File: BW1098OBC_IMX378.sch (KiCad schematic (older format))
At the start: 29 parts, among them J2 24-5804-030-000-829+

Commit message: Update
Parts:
- renumbered 1V05_IMX378_3 to 1V05_IMX378_?, 1V05_IMX378_2 to 1V05_IMX378_?, 1V05_IMX378 to 1V05_IMX?, 1V8_IMX378_3 to 1V8_IMX378_?, 1V8_IMX378_2 to 1V8_IMX378_?, 1V8_IMX378 to 1V8_IMX?, 1V8 to 1V?, 1V05 to 1V?, 2V8_IMX378_3 to 2V8_IMX378_?, 2V8_IMX378_2 to 2V8_IMX378_?, 2V8_IMX378 to 2V8_IMX?, 2V8 to 2V?, 2v8 to 2v?, C3 to C?, C2 to C?, C4 to C?, C5 to C?, C6 to C?, C1 to C?, FB3 to FB?, FB2 to FB?, FB1 to FB?, GND_25 to GND_?, GND_24 to GND_?, GND_23 to GND_?, GND_22 to GND_?, GND_21 to GND_?, J2 to J?, R1 to R?
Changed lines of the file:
@@
 $Descr B 17000 11000
 encoding utf-8
-Sheet 1 1
+Sheet 5 8
 Title "BW1098OBC_IMX378-SchDoc"
 Date "12 12 2020"
@@
 DPHYv1.2
 $Comp
-L power:GND 1V05
+L power:GND 1V?
 U 1 1 5FD53070
 P 1200 1600
-F 0 "1V05" H 1200 1740 20  0000 C CNN
+F 0 "1V?" H 1200 1740 20  0000 C CNN
 F 1 "1V05" H 1200 1710 30  0000 C CNN
 F 2 "" H 1200 1600 70  0000 C CNN
@@
 $EndComp
 $Comp
-L power:GND 2V8
+L power:GND 2V?
 U 1 1 5FD5306F
 P 1200 1000
-F 0 "2V8" H 1200 1140 20  0000 C CNN
+F 0 "2V?" H 1200 1140 20  0000 C CNN
 F 1 "2V8" H 1200 1110 30  0000 C CNN
 F 2 "" H 1200 1000 70  0000 C CNN
@@
 GND
 $Comp
-L power:GND 2V8_IMX378
+L power:GND 2V8_IMX?
 U 1 1 5FD5306E
 P 10000 6900
-F 0 "2V8_IMX378" H 10000 7040 20  0000 C CNN
+F 0 "2V8_IMX?" H 10000 7040 20  0000 C CNN
 F 1 "2V8_IMX378" H 10000 7010 30  0000 C CNN
 F 2 "" H 10000 6900 70  0000 C CNN
@@
 $EndComp
 $Comp
-L power:GND 1V8_IMX378
+L power:GND 1V8_IMX?
 U 1 1 5FD5306D
 P 8700 6900
-F 0 "1V8_IMX378" H 8700 7040 20  0000 C CNN
+F 0 "1V8_IMX?" H 8700 7040 20  0000 C CNN
 F 1 "1V8_IMX378" H 8700 7010 30  0000 C CNN
 F 2 "" H 8700 6900 70  0000 C CNN
@@
 $EndComp
 $Comp
-L power:GND 1V8_IMX378_2
+L power:GND 1V8_IMX378_?
 U 1 1 5FD5306C
 P 7600 5700
-F 0 "1V8_IMX378_2" H 7600 5840 20  0000 C CNN
+F 0 "1V8_IMX378_?" H 7600 5840 20  0000 C CNN
 F 1 "1V8_IMX378" H 7600 5810 30  0000 C CNN
 F 2 "" H 7600 5700 70  0000 C CNN
@@
 $EndComp
 $Comp
-L power:GND GND_21
+L power:GND GND_?
 U 1 1 5FD5306B
 P 11500 5200
-F 0 "GND_21" H 11500 5340 20  0000 C CNN
+F 0 "GND_?" H 11500 5340 20  0000 C CNN
 F 1 "GND" H 11500 5310 30  0000 C CNN
 F 2 "" H 11500 5200 70  0000 C CNN
@@
 $EndComp
 $Comp
-L power:GND GND_22
+L power:GND GND_?
 U 1 1 5FD5306A
 P 1100 1900
-F 0 "GND_22" H 1100 1900 20  0000 C CNN
+F 0 "GND_?" H 1100 1900 20  0000 C CNN
 F 1 "GND" H 1100 1830 30  0000 C CNN
 F 2 "" H 1100 1900 70  0000 C CNN
@@
 $EndComp
 $Comp
-L power:GND GND_23
+L power:GND GND_?
 U 1 1 5FD53069
 P 9000 7400
-F 0 "GND_23" H 9000 7400 20  0000 C CNN
+F 0 "GND_?" H 9000 7400 20  0000 C CNN
 F 1 "GND" H 9000 7330 30  0000 C CNN
 F 2 "" H 9000 7400 70  0000 C CNN
@@
 $EndComp
 $Comp
-L power:GND GND_24
+L power:GND GND_?
 U 1 1 5FD53068
 P 7900 6100
-F 0 "GND_24" H 7900 6100 20  0000 C CNN
+F 0 "GND_?" H 7900 6100 20  0000 C CNN
 F 1 "GND" H 7900 6030 30  0000 C CNN
 F 2 "" H 7900 6100 70  0000 C CNN
@@
 $EndComp
 $Comp
-L power:GND GND_25
+L power:GND GND_?
 U 1 1 5FD53067
 P 9900 6100
-F 0 "GND_25" H 9900 6100 20  0000 C CNN
+F 0 "GND_?" H 9900 6100 20  0000 C CNN
 F 1 "GND" H 9900 6030 30  0000 C CNN
 F 2 "" H 9900 6100 70  0000 C CNN
@@
 1V8
 $Comp
-L power:GND 1V8
+L power:GND 1V?
 U 1 1 5FD53066
 P 1200 1300
-F 0 "1V8" H 1200 1440 20  0000 C CNN
+F 0 "1V?" H 1200 1440 20  0000 C CNN
 F 1 "1V8" H 1200 1410 30  0000 C CNN
 F 2 "" H 1200 1300 70  0000 C CNN
@@
 $EndComp
 $Comp
-L power:GND 1V8_IMX378_3
+L power:GND 1V8_IMX378_?
 U 1 1 5FD53065
 P 2400 1300
-F 0 "1V8_IMX378_3" H 2400 1440 20  0001 C CNN
+F 0 "1V8_IMX378_?" H 2400 1440 20  0001 C CNN
 F 1 "1V8_IMX378" H 2400 1350 30  0000 C CNN
 F 2 "" H 2400 1300 70  0000 C CNN
@@
 $EndComp
 $Comp
-L power:GND 2V8_IMX378_2
+L power:GND 2V8_IMX378_?
 U 1 1 5FD53064
 P 7600 5500
-F 0 "2V8_IMX378_2" H 7600 5640 20  0000 C CNN
+F 0 "2V8_IMX378_?" H 7600 5640 20  0000 C CNN
 F 1 "2V8_IMX378" H 7600 5610 30  0000 C CNN
 F 2 "" H 7600 5500 70  0000 C CNN
@@
 $EndComp
 $Comp
-L power:GND 2V8_IMX378_3
+L power:GND 2V8_IMX378_?
 U 1 1 5FD53063
 P 10100 5700
-F 0 "2V8_IMX378_3" H 10100 5840 20  0000 C CNN
+F 0 "2V8_IMX378_?" H 10100 5840 20  0000 C CNN
 F 1 "2V8_IMX378" H 10100 5810 30  0000 C CNN
 F 2 "" H 10100 5700 70  0000 C CNN
@@
 $EndComp
 $Comp
-L power:GND 2v8
+L power:GND 2v?
 U 1 1 5FD53062
 P 2400 1000
-F 0 "2v8" H 2400 1140 20  0001 C CNN
+F 0 "2v?" H 2400 1140 20  0001 C CNN
 F 1 "2V8_IMX378" H 2400 1050 30  0000 C CNN
 F 2 "" H 2400 1000 70  0000 C CNN
@@
 $EndComp
 $Comp
-L power:GND 1V05_IMX378
+L power:GND 1V05_IMX?
 U 1 1 5FD53061
 P 2400 1600
-F 0 "1V05_IMX378" H 2400 1740 20  0001 C CNN
+F 0 "1V05_IMX?" H 2400 1740 20  0001 C CNN
 F 1 "1V05_IMX378" H 2400 1650 30  0000 C CNN
 F 2 "" H 2400 1600 70  0000 C CNN
@@
 $EndComp
 $Comp
-L power:GND 1V05_IMX378_2
+L power:GND 1V05_IMX378_?
 U 1 1 5FD53060
 P 7400 6900
-F 0 "1V05_IMX378_2" H 7400 7040 20  0000 C CNN
+F 0 "1V05_IMX378_?" H 7400 7040 20  0000 C CNN
 F 1 "1V05_IMX378" H 7400 7010 30  0000 C CNN
 F 2 "" H 7400 6900 70  0000 C CNN
@@
 $EndComp
 $Comp
-L power:GND 1V05_IMX378_3
+L power:GND 1V05_IMX378_?
 U 1 1 5FD5305F
 P 7600 5900
-F 0 "1V05_IMX378_3" H 7600 6040 20  0000 C CNN
+F 0 "1V05_IMX378_?" H 7600 6040 20  0000 C CNN
 F 1 "1V05_IMX378" H 7600 6010 30  0000 C CNN
 F 2 "" H 7600 5900 70  0000 C CNN
@@
 Connection ~ 10000 6900
 $Comp
-L BW1098OBC_IMX378-rescue:2508056017Y2--BW1098OBC_IMX378-SchDoc-rescue FB1
+L BW1098OBC_IMX378-rescue:2508056017Y2--BW1098OBC_IMX378-SchDoc-rescue FB?
 U 1 1 5FD5305E
 P 1400 1000
-F 0 "FB1" H 1500 1050 60  0000 L BNN
+F 0 "FB?" H 1500 1050 60  0000 L BNN
 F 1 "600R/100MHz" H 1500 870 60  0000 L BNN
 F 2 "" H 1500 870 60  0000 C CNN
@@
 $EndComp
 $Comp
-L BW1098OBC_IMX378-rescue:GRM155R71A104JA01D--BW1098OBC_IMX378-SchDoc-rescue C1
+L BW1098OBC_IMX378-rescue:GRM155R71A104JA01D--BW1098OBC_IMX378-SchDoc-rescue C?
 U 1 1 5FD5305D
 P 7400 7200
-F 0 "C1" V 7510 7110 60  0000 R TNN
+F 0 "C?" V 7510 7110 60  0000 R TNN
 F 1 "0.1uF 0402" V 7410 7110 60  0000 R TNN
 F 2 "" H 7410 7110 60  0000 C CNN
@@
 $EndComp
 $Comp
-L BW1098OBC_IMX378-rescue:A12N02A-201_Connector--BW1098OBC_IMX378-SchDoc-rescue J2
+L BW1098OBC_IMX378-rescue:A12N02A-201_Connector--BW1098OBC_IMX378-SchDoc-rescue J?
 U 1 1 5FD5305C
 P 8000 6000
-F 0 "J2" H 8200 7600 60  0000 L BNN
+F 0 "J?" H 8200 7600 60  0000 L BNN
 F 1 "24-5804-030-000-829+" H 8200 5900 60  0000 L BNN
 F 2 "" H 8200 5900 60  0000 C CNN
@@
 $EndComp
 $Comp
-L BW1098OBC_IMX378-rescue:2508056017Y2--BW1098OBC_IMX378-SchDoc-rescue FB2
+L BW1098OBC_IMX378-rescue:2508056017Y2--BW1098OBC_IMX378-SchDoc-rescue FB?
 U 1 1 5FD5305B
 P 1400 1300
-F 0 "FB2" H 1500 1350 60  0000 L BNN
+F 0 "FB?" H 1500 1350 60  0000 L BNN
 F 1 "600R/100MHz" H 1500 1170 60  0000 L BNN
 F 2 "" H 1500 1170 60  0000 C CNN
@@
 $EndComp
 $Comp
-L BW1098OBC_IMX378-rescue:2508056017Y2--BW1098OBC_IMX378-SchDoc-rescue FB3
+L BW1098OBC_IMX378-rescue:2508056017Y2--BW1098OBC_IMX378-SchDoc-rescue FB?
 U 1 1 5FD5305A
 P 1400 1600
-F 0 "FB3" H 1500 1650 60  0000 L BNN
+F 0 "FB?" H 1500 1650 60  0000 L BNN
 F 1 "600R/100MHz" H 1500 1470 60  0000 L BNN
 F 2 "" H 1500 1470 60  0000 C CNN
@@
 $EndComp
 $Comp
-L BW1098OBC_IMX378-rescue:RC0402FR-1310KL--BW1098OBC_IMX378-SchDoc-rescue R1
+L BW1098OBC_IMX378-rescue:RC0402FR-1310KL--BW1098OBC_IMX378-SchDoc-rescue R?
 U 1 1 5FD53059
 P 11000 5200
-F 0 "R1" H 11090 5230 60  0000 L BNN
+F 0 "R?" H 11090 5230 60  0000 L BNN
 F 1 "10K 0402" H 11090 5070 60  0000 L BNN
 F 2 "" H 11090 5070 60  0000 C CNN
@@
 $EndComp
 $Comp
-L BW1098OBC_IMX378-rescue:GRM188R61A106ME69D--BW1098OBC_IMX378-SchDoc-rescue C6
+L BW1098OBC_IMX378-rescue:GRM188R61A106ME69D--BW1098OBC_IMX378-SchDoc-rescue C?
 U 1 1 5FD53058
 P 10600 7200
-F 0 "C6" V 10710 7110 60  0000 R TNN
+F 0 "C?" V 10710 7110 60  0000 R TNN
 F 1 "10uF 0603" V 10610 7110 60  0000 R TNN
 F 2 "" H 10610 7110 60  0000 C CNN
@@
 $EndComp
 $Comp
-L BW1098OBC_IMX378-rescue:GRM155R71A104JA01D--BW1098OBC_IMX378-SchDoc-rescue C5
+L BW1098OBC_IMX378-rescue:GRM155R71A104JA01D--BW1098OBC_IMX378-SchDoc-rescue C?
 U 1 1 5FD53057
 P 10000 7200
-F 0 "C5" V 10110 7110 60  0000 R TNN
+F 0 "C?" V 10110 7110 60  0000 R TNN
 F 1 "0.1uF 0402" V 10010 7110 60  0000 R TNN
 F 2 "" H 10010 7110 60  0000 C CNN
@@
 $EndComp
 $Comp
-L BW1098OBC_IMX378-rescue:GRM188R61A106ME69D--BW1098OBC_IMX378-SchDoc-rescue C4
+L BW1098OBC_IMX378-rescue:GRM188R61A106ME69D--BW1098OBC_IMX378-SchDoc-rescue C?
 U 1 1 5FD53056
 P 9300 7200
-F 0 "C4" V 9410 7110 60  0000 R TNN
+F 0 "C?" V 9410 7110 60  0000 R TNN
 F 1 "10uF 0603" V 9310 7110 60  0000 R TNN
 F 2 "" H 9310 7110 60  0000 C CNN
@@
 $EndComp
 $Comp
-L BW1098OBC_IMX378-rescue:GRM188R61A106ME69D--BW1098OBC_IMX378-SchDoc-rescue C2
+L BW1098OBC_IMX378-rescue:GRM188R61A106ME69D--BW1098OBC_IMX378-SchDoc-rescue C?
 U 1 1 5FD53055
 P 8000 7200
-F 0 "C2" V 8110 7110 60  0000 R TNN
+F 0 "C?" V 8110 7110 60  0000 R TNN
 F 1 "10uF 0603" V 8010 7110 60  0000 R TNN
 F 2 "" H 8010 7110 60  0000 C CNN
@@
 $EndComp
 $Comp
-L BW1098OBC_IMX378-rescue:GRM155R71A104JA01D--BW1098OBC_IMX378-SchDoc-rescue C3
+L BW1098OBC_IMX378-rescue:GRM155R71A104JA01D--BW1098OBC_IMX378-SchDoc-rescue C?
 U 1 1 5FD53054
 P 8700 7200
-F 0 "C3" V 8810 7110 60  0000 R TNN
+F 0 "C?" V 8810 7110 60  0000 R TNN
 F 1 "0.1uF 0402" V 8710 7110 60  0000 R TNN
 F 2 "" H 8710 7110 60  0000 C CNN

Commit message: Cleaned up some duplicates, started reorganizing and putting symbols into one luxonis library so the others can be deleted, added SOM Connector footprint
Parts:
- C? (x3): symbol BW1098OBC_IMX378-rescue:GRM155R71A104JA01D--BW1098OBC_IMX378-SchDoc-rescue -> BW1098OBC_TopLevel-rescue:GRM155R71A104JA01D--BW1098OBC_IMX378-SchDoc-rescue-BW1098OBC_IMX378-rescue
- C? (x3): symbol BW1098OBC_IMX378-rescue:GRM188R61A106ME69D--BW1098OBC_IMX378-SchDoc-rescue -> BW1098OBC_TopLevel-rescue:GRM188R61A106ME69D--BW1098OBC_IMX378-SchDoc-rescue-BW1098OBC_IMX378-rescue
- FB? (x3): symbol BW1098OBC_IMX378-rescue:2508056017Y2--BW1098OBC_IMX378-SchDoc-rescue -> BW1098OBC_TopLevel-rescue:2508056017Y2--BW1098OBC_IMX378-SchDoc-rescue-BW1098OBC_IMX378-rescue
- J?: symbol BW1098OBC_IMX378-rescue:A12N02A-201_Connector--BW1098OBC_IMX378-SchDoc-rescue -> BW1098OBC_TopLevel-rescue:A12N02A-201_Connector--BW1098OBC_IMX378-SchDoc-rescue-BW1098OBC_IMX378-rescue
- R?: symbol BW1098OBC_IMX378-rescue:RC0402FR-1310KL--BW1098OBC_IMX378-SchDoc-rescue -> BW1098OBC_TopLevel-rescue:RC0402FR-1310KL--BW1098OBC_IMX378-SchDoc-rescue-BW1098OBC_IMX378-rescue
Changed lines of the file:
@@
 Connection ~ 10000 6900
 $Comp
-L BW1098OBC_IMX378-rescue:2508056017Y2--BW1098OBC_IMX378-SchDoc-rescue FB?
+L BW1098OBC_TopLevel-rescue:2508056017Y2--BW1098OBC_IMX378-SchDoc-rescue-BW1098OBC_IMX378-rescue FB?
 U 1 1 5FD5305E
 P 1400 1000
@@
 $EndComp
 $Comp
-L BW1098OBC_IMX378-rescue:GRM155R71A104JA01D--BW1098OBC_IMX378-SchDoc-rescue C?
+L BW1098OBC_TopLevel-rescue:GRM155R71A104JA01D--BW1098OBC_IMX378-SchDoc-rescue-BW1098OBC_IMX378-rescue C?
 U 1 1 5FD5305D
 P 7400 7200
@@
 $EndComp
 $Comp
-L BW1098OBC_IMX378-rescue:A12N02A-201_Connector--BW1098OBC_IMX378-SchDoc-rescue J?
+L BW1098OBC_TopLevel-rescue:A12N02A-201_Connector--BW1098OBC_IMX378-SchDoc-rescue-BW1098OBC_IMX378-rescue J?
 U 1 1 5FD5305C
 P 8000 6000
@@
 $EndComp
 $Comp
-L BW1098OBC_IMX378-rescue:2508056017Y2--BW1098OBC_IMX378-SchDoc-rescue FB?
+L BW1098OBC_TopLevel-rescue:2508056017Y2--BW1098OBC_IMX378-SchDoc-rescue-BW1098OBC_IMX378-rescue FB?
 U 1 1 5FD5305B
 P 1400 1300
@@
 $EndComp
 $Comp
-L BW1098OBC_IMX378-rescue:2508056017Y2--BW1098OBC_IMX378-SchDoc-rescue FB?
+L BW1098OBC_TopLevel-rescue:2508056017Y2--BW1098OBC_IMX378-SchDoc-rescue-BW1098OBC_IMX378-rescue FB?
 U 1 1 5FD5305A
 P 1400 1600
@@
 $EndComp
 $Comp
-L BW1098OBC_IMX378-rescue:RC0402FR-1310KL--BW1098OBC_IMX378-SchDoc-rescue R?
+L BW1098OBC_TopLevel-rescue:RC0402FR-1310KL--BW1098OBC_IMX378-SchDoc-rescue-BW1098OBC_IMX378-rescue R?
 U 1 1 5FD53059
 P 11000 5200
@@
 $EndComp
 $Comp
-L BW1098OBC_IMX378-rescue:GRM188R61A106ME69D--BW1098OBC_IMX378-SchDoc-rescue C?
+L BW1098OBC_TopLevel-rescue:GRM188R61A106ME69D--BW1098OBC_IMX378-SchDoc-rescue-BW1098OBC_IMX378-rescue C?
 U 1 1 5FD53058
 P 10600 7200
@@
 $EndComp
 $Comp
-L BW1098OBC_IMX378-rescue:GRM155R71A104JA01D--BW1098OBC_IMX378-SchDoc-rescue C?
+L BW1098OBC_TopLevel-rescue:GRM155R71A104JA01D--BW1098OBC_IMX378-SchDoc-rescue-BW1098OBC_IMX378-rescue C?
 U 1 1 5FD53057
 P 10000 7200
@@
 $EndComp
 $Comp
-L BW1098OBC_IMX378-rescue:GRM188R61A106ME69D--BW1098OBC_IMX378-SchDoc-rescue C?
+L BW1098OBC_TopLevel-rescue:GRM188R61A106ME69D--BW1098OBC_IMX378-SchDoc-rescue-BW1098OBC_IMX378-rescue C?
 U 1 1 5FD53056
 P 9300 7200
@@
 $EndComp
 $Comp
-L BW1098OBC_IMX378-rescue:GRM188R61A106ME69D--BW1098OBC_IMX378-SchDoc-rescue C?
+L BW1098OBC_TopLevel-rescue:GRM188R61A106ME69D--BW1098OBC_IMX378-SchDoc-rescue-BW1098OBC_IMX378-rescue C?
 U 1 1 5FD53055
 P 8000 7200
@@
 $EndComp
 $Comp
-L BW1098OBC_IMX378-rescue:GRM155R71A104JA01D--BW1098OBC_IMX378-SchDoc-rescue C?
+L BW1098OBC_TopLevel-rescue:GRM155R71A104JA01D--BW1098OBC_IMX378-SchDoc-rescue-BW1098OBC_IMX378-rescue C?
 U 1 1 5FD53054
 P 8700 7200

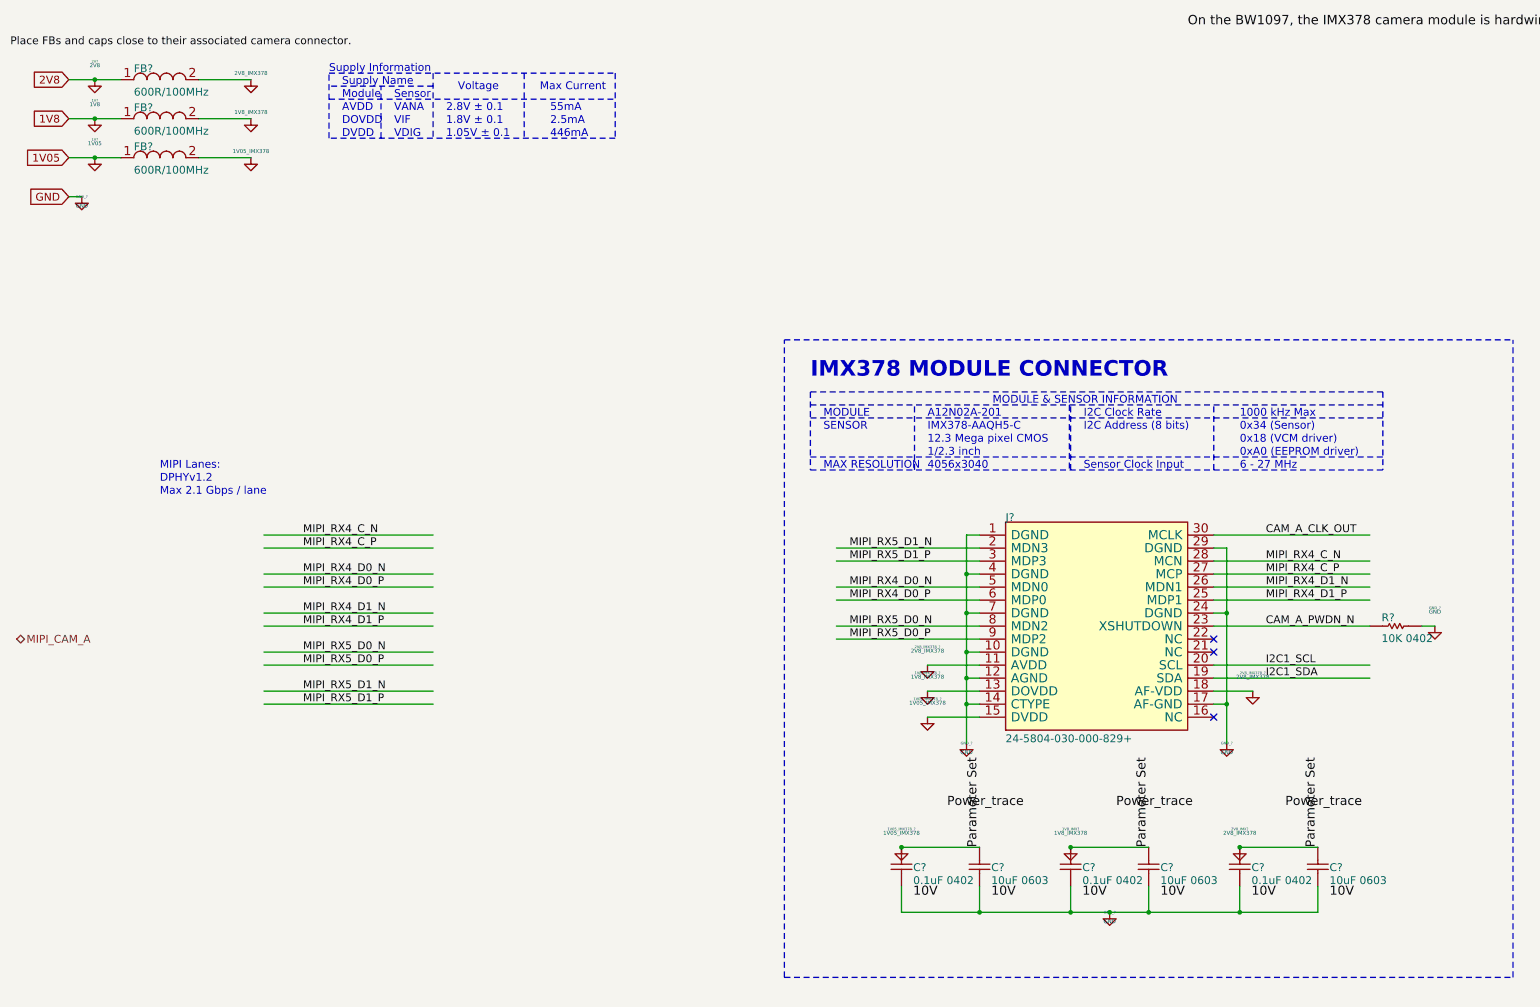
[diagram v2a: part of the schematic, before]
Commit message: More deletion of corrupted or duplicate files, added footprints and associations for mounting holes and 30 pin connector
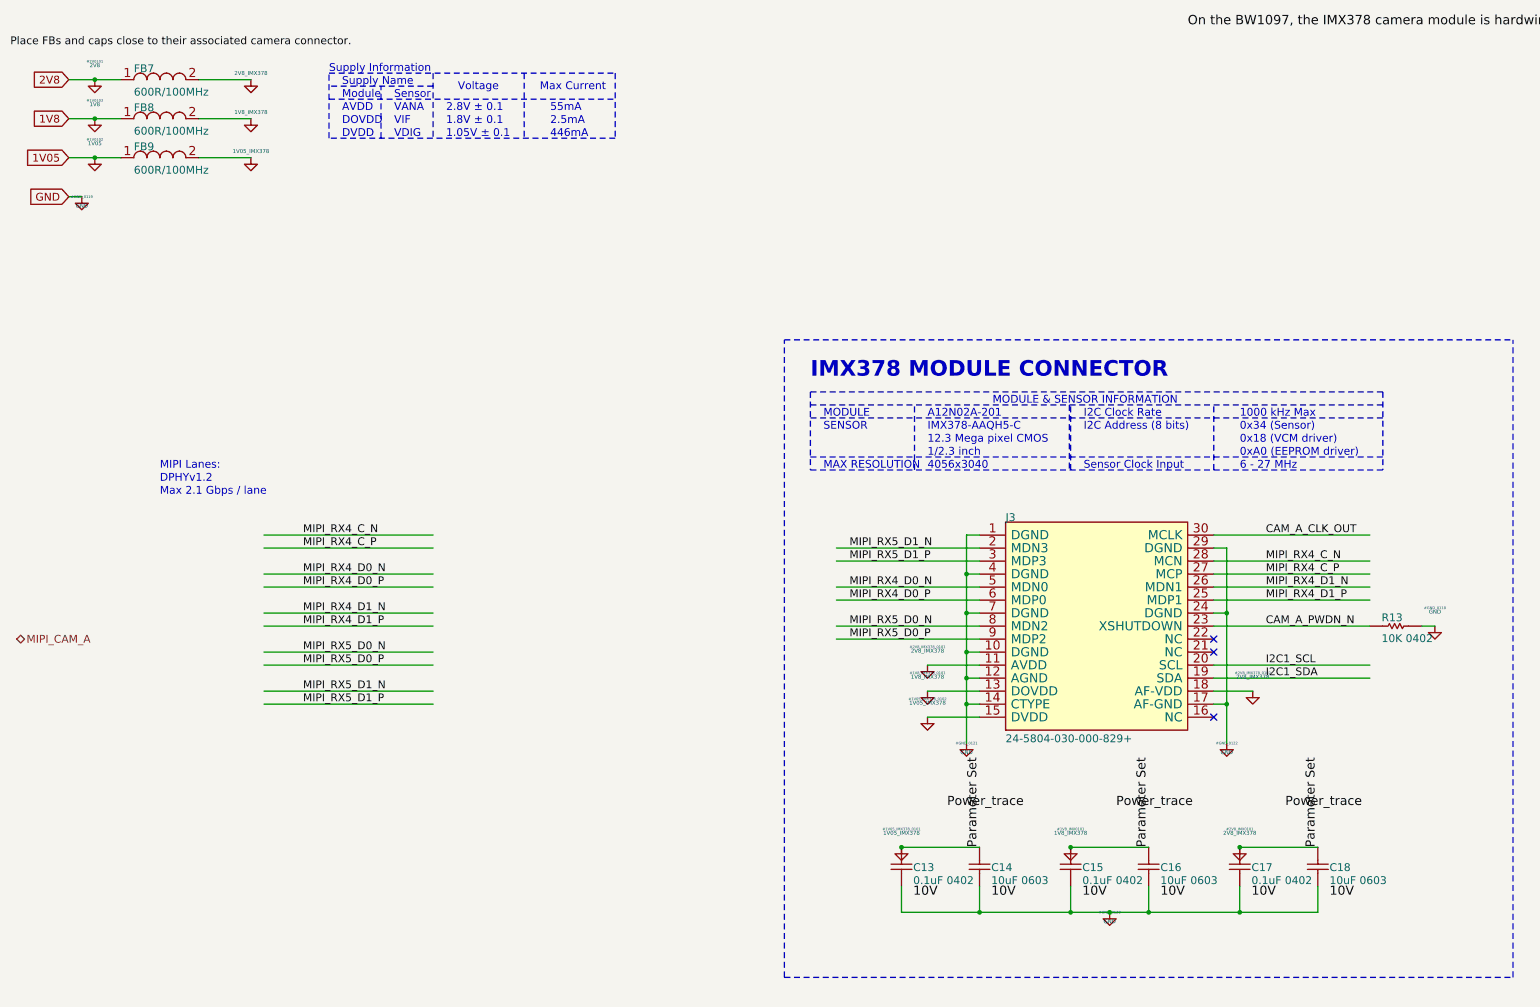
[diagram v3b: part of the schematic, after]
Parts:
- removed 1V05_IMX378_? (x2), 1V05_IMX?: 1V05_IMX378, symbol power:GND
- removed 1V8_IMX378_? (x2), 1V8_IMX?: 1V8_IMX378, symbol power:GND
- removed 1V?: 1V8, symbol power:GND
- removed 1V?: 1V05, symbol power:GND
- removed 2V8_IMX378_? (x2), 2V8_IMX?, 2v?: 2V8_IMX378, symbol power:GND
- removed 2V?: 2V8, symbol power:GND
- removed GND_? (x5): GND, symbol power:GND
- J3: renamed from J?; footprint (none) -> fp_luxonis:245804030000829
- gave numbers to parts that had none: 10
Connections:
- net labels added: 1V05_IMX378, 1V8_IMX378, 2V8_IMX378
